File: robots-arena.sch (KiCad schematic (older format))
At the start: 32 parts

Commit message: added bat mgmt, pwr select, xbee header
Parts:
- removed SW?: DIPS_02, symbol DIPS_02
- added P?: CONN_01X09, symbol CONN_01X09
- added R? (x2): 330, symbol R
- added R?: 50k, symbol R
- added SW?: SW_PUSH, symbol SW_PUSH
- added SW?: DIPSW_02, symbol DIPSW_02
- added U?: XBee_Header, symbol XBee_Header
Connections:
- net labels added: BEE_DTR, UART_5_CTS, UART_5_RTS, UART_5_RX, UART_5_TX
- wire segments 153 -> 158
- no-connect marks 24 -> 29
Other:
- note added: "XBee/GPRS Bee Expansion Header"

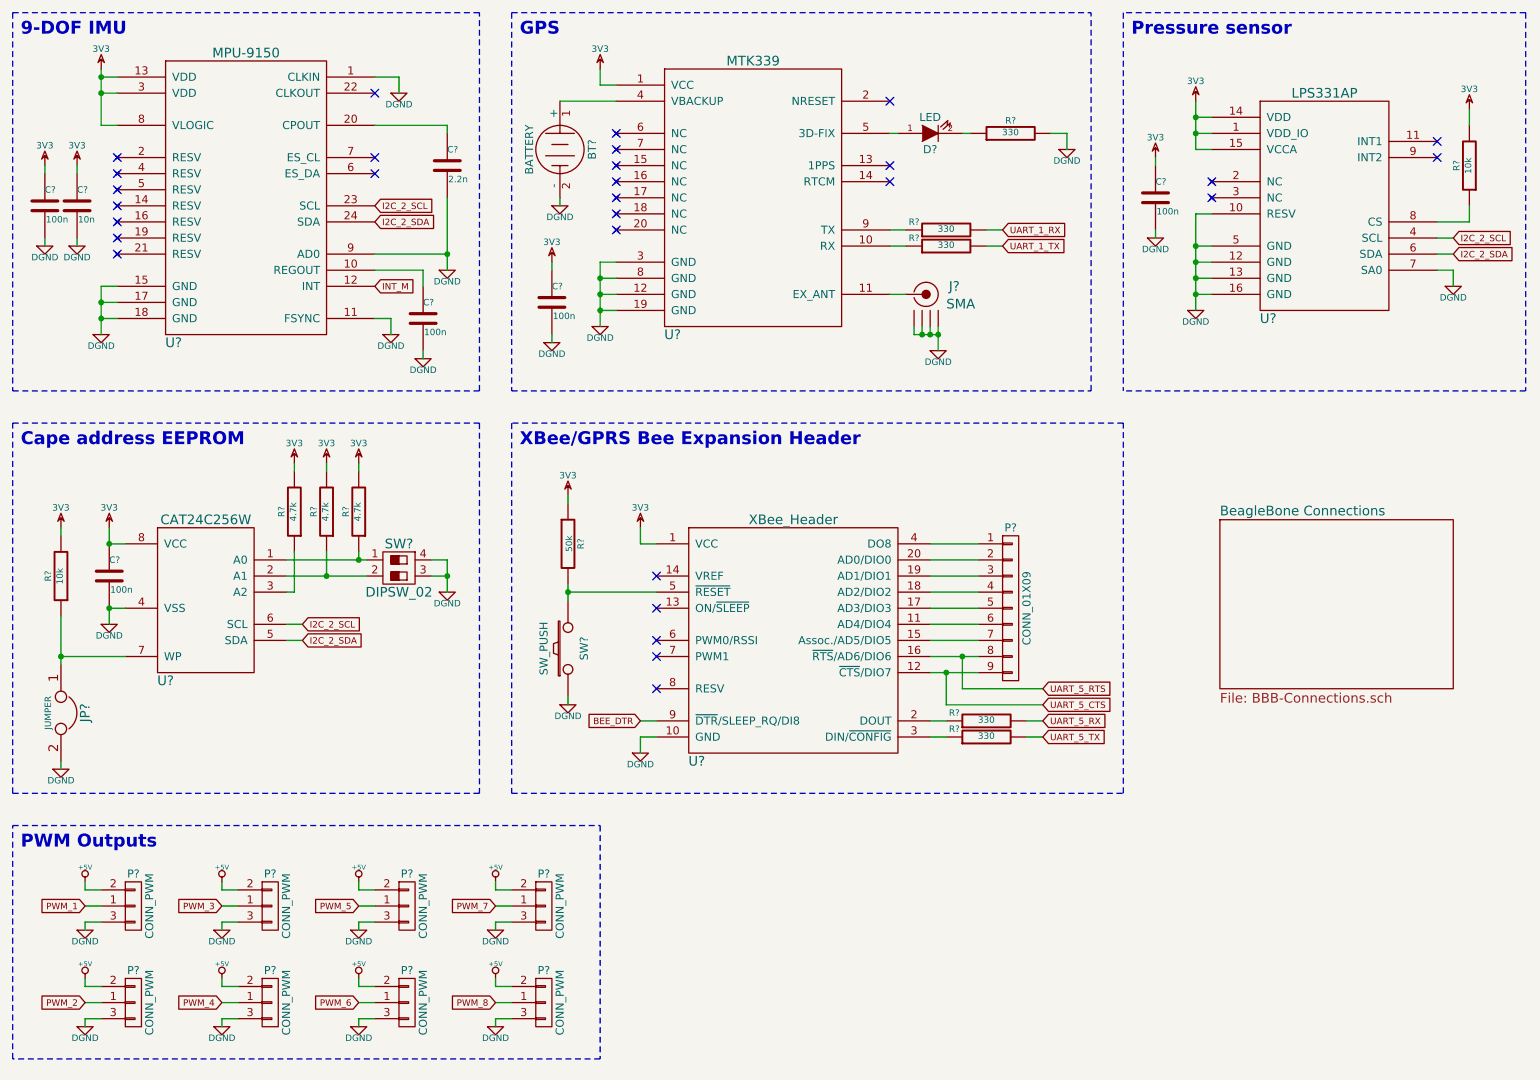
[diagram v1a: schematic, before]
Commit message: .sch done, .net done, components on PCB done
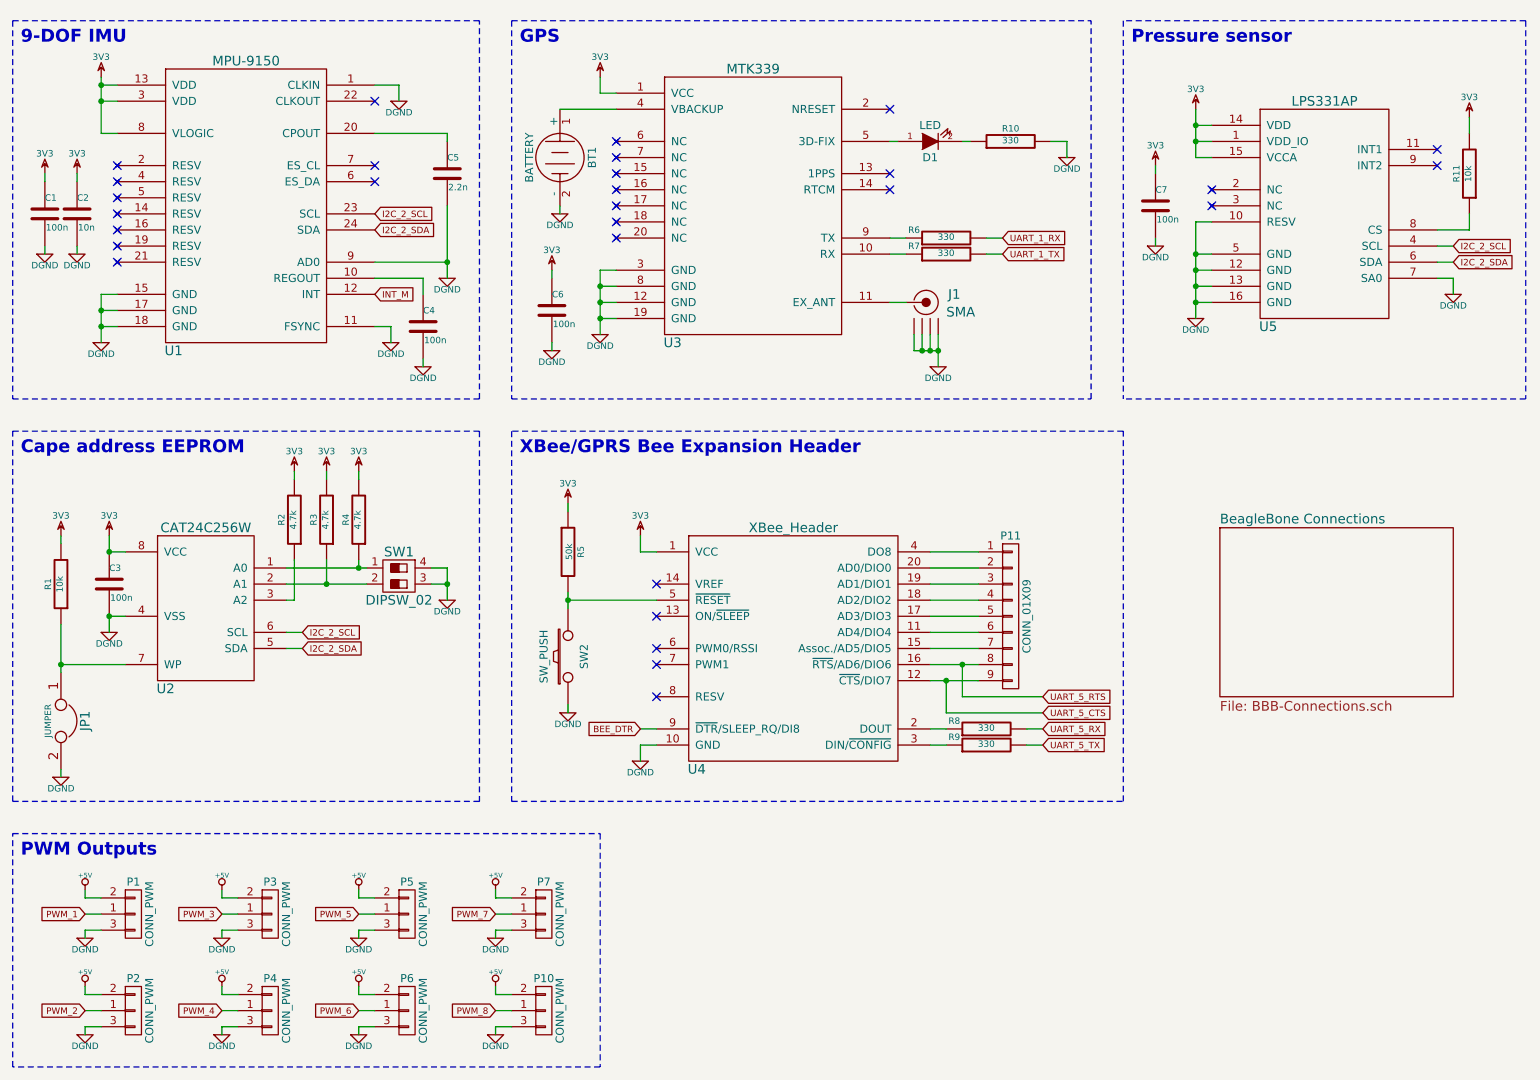
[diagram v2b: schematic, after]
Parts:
- gave numbers to parts that had none: 38
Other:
- moved on the sheet: BT1, C1, C2, C3, C4, C5, C6, C7, D1, J1, JP1, P1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

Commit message: Added adc connectors w/ 5 to 1.8V conversion
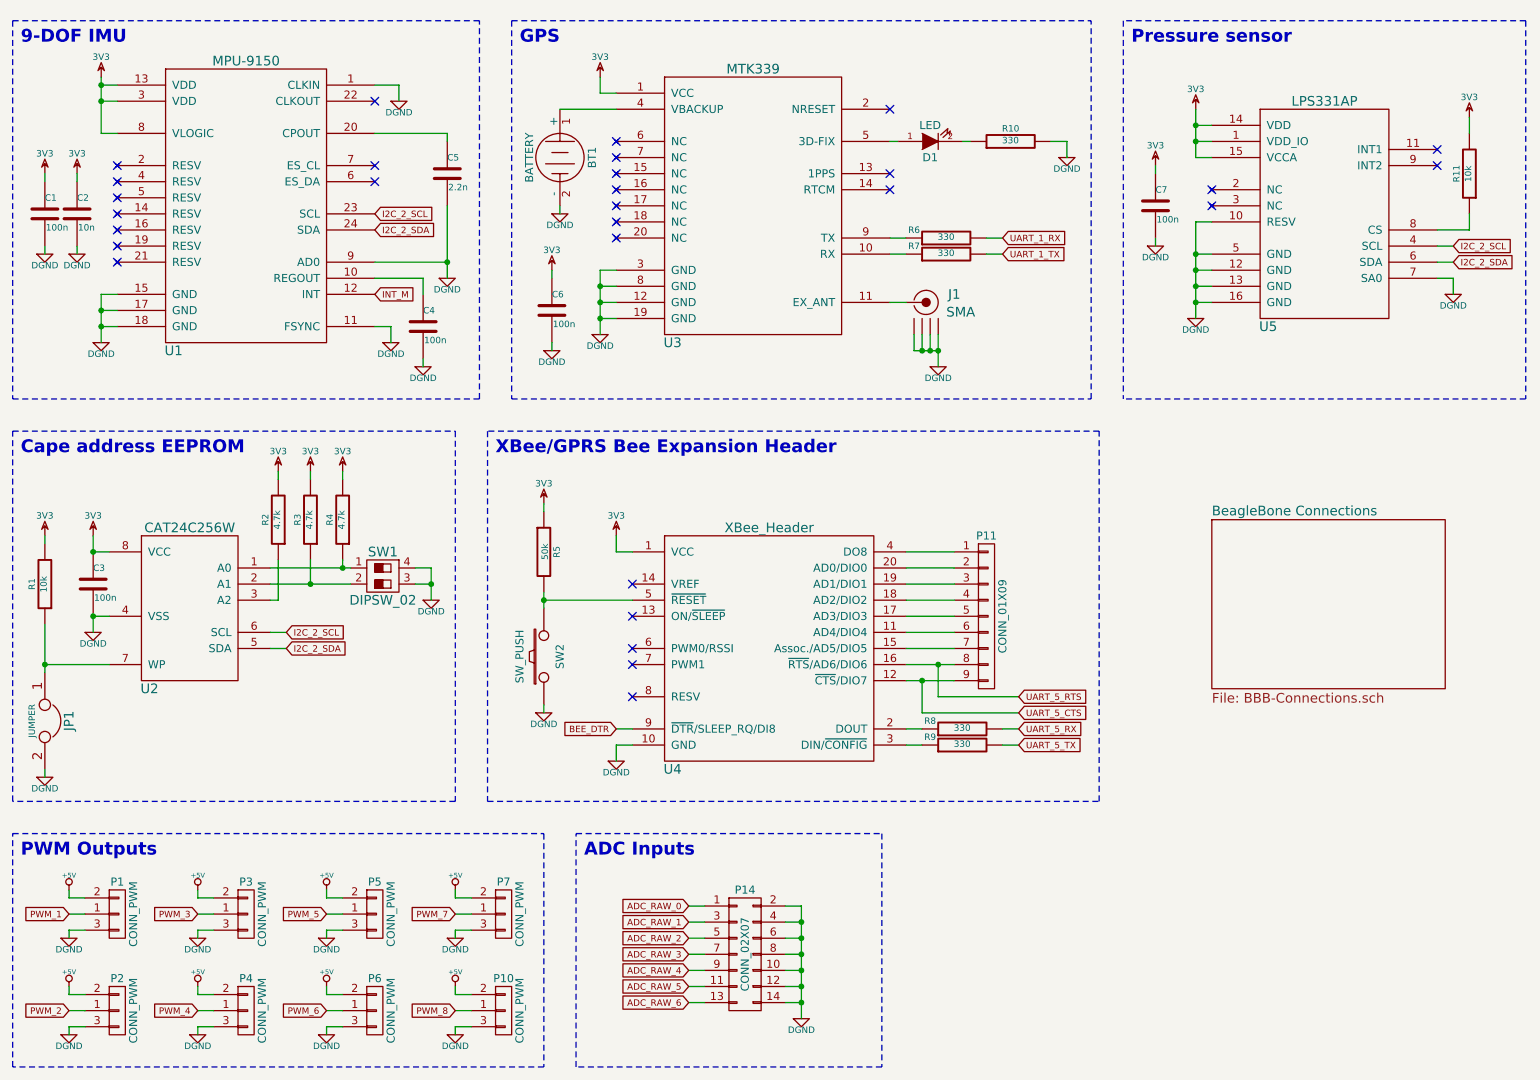
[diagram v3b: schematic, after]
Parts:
- added P14: CONN_02X07, symbol CONN_02X07
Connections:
- net DGND: now also P14.10 (P10), P14.12 (P12), P14.14 (P14), P14.2 (P2), P14.4 (P4), P14.6 (P6), P14.8 (P8)
- new net ADC_RAW_0: P14.1 (P1)
- new net ADC_RAW_1: P14.3 (P3)
- new net ADC_RAW_2: P14.5 (P5)
- new net ADC_RAW_3: P14.7 (P7)
- new net ADC_RAW_4: P14.9 (P9)
- new net ADC_RAW_5: P14.11 (P11)
- new net ADC_RAW_6: P14.13 (P13)
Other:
- note added: "ADC Inputs"
- moved on the sheet: C3, JP1, P1, P10, P11, P2, P3, P4, P5, P6, P7, R1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

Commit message: Added comments on the schematics
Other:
- note added: "Accepts 5V input signals"
- moved on the sheet: C3, JP1, P11, R1, R2, R3, R4, R5, R8, R9, SW1, SW2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

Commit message: Update netlist & components footprints
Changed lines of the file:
@@
 $EndComp
 Wire Wire Line
-	3850 2000 3850 2350
-Wire Wire Line
-	3850 2350 3850 2450
+	3850 2000 3850 2450
 Wire Wire Line
 	3700 2950 3700 3000
@@
 	1700 2750 1800 2750
 Wire Wire Line
-	1700 2550 1700 2650
-Wire Wire Line
-	1700 2650 1700 2750
-Wire Wire Line
-	1700 2750 1700 2850
+	1700 2550 1700 2850
 Wire Wire Line
 	1700 2650 1800 2650
@@
 Connection ~ 1700 2650
 Wire Wire Line
-	1700 1200 1700 1250
-Wire Wire Line
-	1700 1250 1700 1350
-Wire Wire Line
-	1700 1350 1700 1550
+	1700 1200 1700 1550
 Wire Wire Line
 	1700 1250 1800 1250
@@
 	4800 2700 4900 2700
 Wire Wire Line
-	4800 2400 4800 2500
-Wire Wire Line
-	4800 2500 4800 2600
-Wire Wire Line
-	4800 2600 4800 2700
-Wire Wire Line
-	4800 2700 4800 2800
+	4800 2400 4800 2800
 Wire Wire Line
 	4800 2600 4900 2600
@@
 	8500 2600 8600 2600
 Wire Wire Line
-	8500 2100 8500 2300
-Wire Wire Line
-	8500 2300 8500 2400
-Wire Wire Line
-	8500 2400 8500 2500
-Wire Wire Line
-	8500 2500 8500 2600
-Wire Wire Line
-	8500 2600 8500 2700
+	8500 2100 8500 2700
 Wire Wire Line
 	8600 2500 8500 2500
@@
 Connection ~ 8500 2300
 Wire Wire Line
-	8500 1400 8500 1500
-Wire Wire Line
-	8500 1500 8500 1600
-Wire Wire Line
-	8500 1600 8500 1700
+	8500 1400 8500 1700
 Wire Wire Line
 	8500 1500 8600 1500
@@
 	1850 4850 1450 4850
 Wire Wire Line
-	1450 4600 1450 4850
-Wire Wire Line
-	1450 4850 1450 4900
+	1450 4600 1450 4900
 Connection ~ 1450 4850
 Wire Wire Line
@@
 	2900 4450 2900 4200
 Wire Wire Line
-	2850 4250 3300 4250
-Wire Wire Line
-	3300 4250 3350 4250
+	2850 4250 3350 4250
 Wire Wire Line
 	3300 4250 3300 4200
 Wire Wire Line
-	2850 4350 3100 4350
-Wire Wire Line
-	3100 4350 3350 4350
+	2850 4350 3350 4350
 Wire Wire Line
 	3100 4350 3100 4200
@@
 Connection ~ 3100 4350
 Wire Wire Line
-	3850 4250 3850 4350
-Wire Wire Line
-	3850 4350 3850 4450
+	3850 4250 3850 4450
 Wire Wire Line
 	3850 4350 3750 4350
@@
 	7200 4750 6900 4750
 Wire Wire Line
-	6900 4850 7100 4850
-Wire Wire Line
-	7100 4850 7200 4850
-Wire Wire Line
-	6900 4950 7000 4950
-Wire Wire Line
-	7000 4950 7200 4950
+	6900 4850 7200 4850
+Wire Wire Line
+	6900 4950 7200 4950
 Text GLabel 7600 5150 2    40   Input ~ 0
 UART_5_CTS
@@
 $EndComp
 Wire Wire Line
-	4650 4400 4650 4450
-Wire Wire Line
-	4650 4450 4650 4500
+	4650 4400 4650 4500
 Wire Wire Line
 	4650 4450 5200 4450
@@
 	6600 2600 6700 2600
 Wire Wire Line
-	6900 2800 6900 2900
-Wire Wire Line
-	6900 2900 6900 3000
+	6900 2800 6900 3000
 Wire Wire Line
 	6850 2900 6850 2800
 Wire Wire Line
-	6750 2900 6800 2900
-Wire Wire Line
-	6800 2900 6850 2900
-Wire Wire Line
-	6850 2900 6900 2900
+	6750 2900 6900 2900
 Connection ~ 6900 2900
 Wire Wire Line
@@
 $EndComp
 Wire Wire Line
-	6050 6350 6050 6450
-Wire Wire Line
-	6050 6450 6050 6550
-Wire Wire Line
-	6050 6550 6050 6650
-Wire Wire Line
-	6050 6650 6050 6750
-Wire Wire Line
-	6050 6750 6050 6850
-Wire Wire Line
-	6050 6850 6050 6950
-Wire Wire Line
-	6050 6950 6050 7050
+	6050 6350 6050 7050
 Wire Wire Line
 	6050 6950 5950 6950

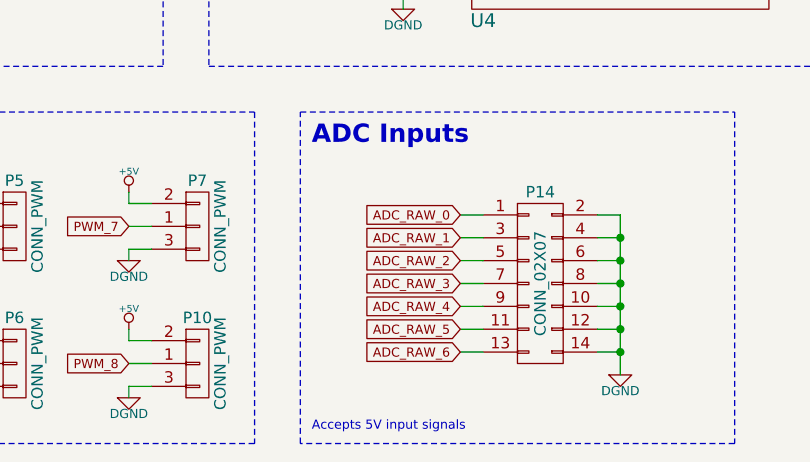
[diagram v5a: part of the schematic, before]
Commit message: Place components on PCB & ajust nets to stay w/ 2 layers
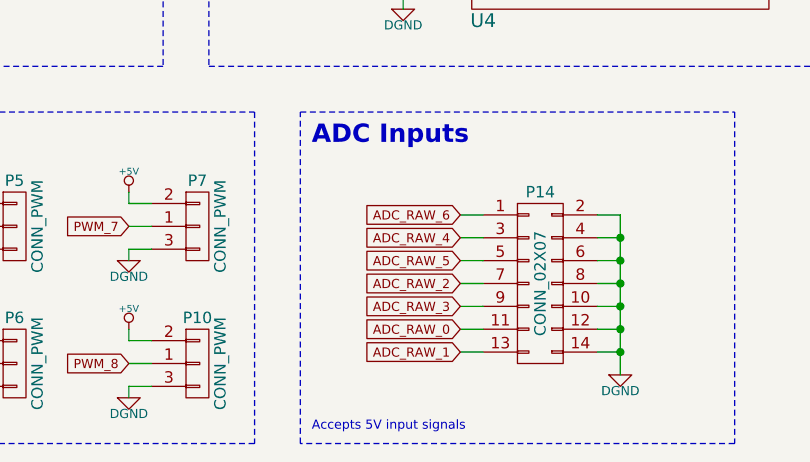
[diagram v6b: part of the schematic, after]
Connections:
- net ADC_RAW_0: now also P14.11 (P11); no longer P14.1 (P1)
- net ADC_RAW_1: now also P14.13 (P13); no longer P14.3 (P3)
- net ADC_RAW_2: now also P14.7 (P7); no longer P14.5 (P5)
- net ADC_RAW_3: now also P14.9 (P9); no longer P14.7 (P7)
- net ADC_RAW_4: now also P14.3 (P3); no longer P14.9 (P9)
- net ADC_RAW_5: now also P14.5 (P5); no longer P14.11 (P11)
- net ADC_RAW_6: now also P14.1 (P1); no longer P14.13 (P13)
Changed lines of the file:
@@
 	5950 6350 6050 6350
 Connection ~ 6050 6450
+Text GLabel 5350 6850 0    40   Input ~ 0
+ADC_RAW_0
+Text GLabel 5350 6950 0    40   Input ~ 0
+ADC_RAW_1
+Text GLabel 5350 6650 0    40   Input ~ 0
+ADC_RAW_2
+Text GLabel 5350 6750 0    40   Input ~ 0
+ADC_RAW_3
+Text GLabel 5350 6450 0    40   Input ~ 0
+ADC_RAW_4
+Text GLabel 5350 6550 0    40   Input ~ 0
+ADC_RAW_5
 Text GLabel 5350 6350 0    40   Input ~ 0
-ADC_RAW_0
-Text GLabel 5350 6450 0    40   Input ~ 0
-ADC_RAW_1
-Text GLabel 5350 6550 0    40   Input ~ 0
-ADC_RAW_2
-Text GLabel 5350 6650 0    40   Input ~ 0
-ADC_RAW_3
-Text GLabel 5350 6750 0    40   Input ~ 0
-ADC_RAW_4
-Text GLabel 5350 6850 0    40   Input ~ 0
-ADC_RAW_5
-Text GLabel 5350 6950 0    40   Input ~ 0
 ADC_RAW_6
 Wire Wire Line
